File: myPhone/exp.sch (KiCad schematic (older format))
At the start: 19 parts, among them J301 iMX8

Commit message: upgrade to kicad 5; fixed footprints
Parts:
- C301, C302, C303, C304, C305, C306, C307, C308, C309, C310, C311, C312, C313, C314, C315, C316, C317, C318: footprint Capacitors_SMD:C_0603 -> Capacitor_SMD:C_0603_1608Metric; symbol C -> Device:C
- J301: symbol iMX8 -> SODIMM-204:iMX8

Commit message: REV1 board
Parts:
- added C319, C321, C325, C327, C337, C339: 1uF, Capacitor_SMD:C_0603_1608Metric, symbol Device:C_Small
- added C320, C322, C323, C326, C328, C329, C331, C333, C335, C338, C340: 0.1uF, Capacitor_SMD:C_0603_1608Metric, symbol Device:C_Small
- added C324, C330, C332, C334, C336: 0.01uF, Capacitor_SMD:C_0603_1608Metric, symbol Device:C_Small
- added C341, C342: 0.1uF, Capacitor_SMD:C_0603_1608Metric, symbol Device:C
- added J302: Touch, Connector_FFC-FPC:Hirose_FH12-6S-0.5SH_1x06-1MP_P0.50mm_Horizontal, symbol Connector_Generic:Conn_01x06
- added J303: Display, Connector_FFC-FPC:Hirose_FH12-40S-0.5SH_1x40-1MP_P0.50mm_Horizontal, symbol Connector_Generic:Conn_01x40
- added J304: Prog, Connector_FFC-FPC:Hirose_FH12-12S-0.5SH_1x12-1MP_P0.50mm_Horizontal, symbol Connector_Generic:Conn_01x12
- added R301: 4.7K, Resistor_SMD:R_0603_1608Metric, symbol Device:R
- added R302, R303: 1K, Resistor_SMD:R_0603_1608Metric, symbol Device:R
- added R304: 100K, Resistor_SMD:R_0603_1608Metric, symbol Device:R
- added U301: SN65LVDS822_SWAP, Package_DFN_QFN:QFN-48-1EP_7x7mm_P0.5mm_EP5.15x5.15mm_ThermalVias, symbol sn65:SN65LVDS822_SWAP
- added U302, U303, U304: TS3DDR3812, footprints:Texas_R-PWQFN-N42, symbol ts3ddr:TS3DDR3812
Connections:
- net GND: now also C319.2, C320.2, C321.2, C322.2, C323.2, C324.2, C325.2, C326.2, C327.2, C328.2, C329.2, C330.2, C331.2, C332.2, C333.2, C334.2, C335.2, C336.2, C337.2, C338.2, C339.2, C340.2, C341.2, C342.2, J302.6 (Pin_6), J303.29 (Pin_29), J303.3 (Pin_3), J303.36 (Pin_36), J304.3 (Pin_3), J304.9 (Pin_9), R304.2, U301.36 (MODE14), U301.49 (GND), U302.43 (GND), U303.43 (GND), U304.43 (GND)
- net iMX8_I2C1_SCL: now reaches J301.129 (PIN129)
- net iMX8_I2C1_SCL: now also U302.34 (B4)
- net iMX8_I2C1_SDA: now reaches J301.135 (PIN135)
- net iMX8_I2C1_SDA: now also U302.32 (B5)
- net iMX8_GPIO3_IO13: now reaches J301.149 (PIN149)
- net iMX8_GPIO3_IO13: now also U302.10 (SEL2), U302.9 (SEL1), U303.10 (SEL2), U303.9 (SEL1), U304.10 (SEL2), U304.9 (SEL1)
- net iMX8_GPIO3_IO12: now reaches J301.151 (PIN151)
- net iMX8_GPIO3_IO12: now also U302.38 (B2)
- net iMX8_GPIO3_IO11: now reaches J301.153 (PIN153)
- net iMX8_GPIO3_IO11: now also U302.36 (B3)
- net iMX8_USB1_D_P: now reaches J301.176 (PIN176)
- net iMX8_USB1_D_N: now reaches J301.178 (PIN178)
- net iMX8_LVDS0_CLK_P: now reaches J301.33 (PIN33)
- net iMX8_LVDS0_CLK_P: now also U301.32 (CLKP)
- net iMX8_LVDS0_CLK_N: now reaches J301.35 (PIN35)
- net iMX8_LVDS0_CLK_N: now also U301.31 (CLKN)
- net iMX8_LVDS0_A0_P: now reaches J301.39 (PIN39)
- net iMX8_LVDS0_A0_P: now also U301.26 (A0P)
- net iMX8_LVDS0_A0_N: now reaches J301.41 (PIN41)
- net iMX8_LVDS0_A0_N: now also U301.25 (A0N)
- net iMX8_LVDS0_A1_P: now reaches J301.45 (PIN45)
- net iMX8_LVDS0_A1_P: now also U301.28 (A1P)
- net iMX8_LVDS0_A1_N: now reaches J301.47 (PIN47)
- net iMX8_LVDS0_A1_N: now also U301.27 (A1N)
- net iMX8_GPIO5_IO28: now reaches J301.5 (PIN5)
- net iMX8_GPIO5_IO28: now also U304.25 (B8)
- net iMX8_LVDS0_A2_P: now reaches J301.51 (PIN51)
- net iMX8_LVDS0_A2_P: now also U301.30 (A2P)
- net iMX8_LVDS0_A2_N: now reaches J301.53 (PIN53)
- net iMX8_LVDS0_A2_N: now also U301.29 (A2N)
- net iMX8_LVDS0_A3_P: now reaches J301.57 (PIN57)
- net iMX8_LVDS0_A3_P: now also U301.34 (A3P)
- net iMX8_GPIO5_IO25: now reaches J301.58 (PIN58)
- net iMX8_GPIO5_IO25: now also U301.23 (CLKPOL)
- net iMX8_LVDS0_A3_N: now reaches J301.59 (PIN59)
- net iMX8_LVDS0_A3_N: now also U301.33 (A3N)
- net iMX8_PWM1: now reaches J301.75 (PIN75)
- net iMX8_PWM1: now also U302.29 (B6)
- net iMX8_GPIO2_IO17: now reaches J301.88 (PIN88)
- net iMX8_GPIO2_IO17: now also U301.35 (SLEW)
- net iMX8_GPIO2_IO18: now reaches J301.90 (PIN90)
- net iMX8_GPIO2_IO18: now also U301.37 (SHTDN#)
- new net +3V3: C319.1, C320.1, C321.1, C322.1, C323.1, C324.1, C325.1, C326.1, C327.1, C328.1, C329.1, C330.1, C331.1, C332.1, C333.1, C334.1, C335.1, C336.1, C337.1, C338.1, C339.1, C340.1, C341.1, C342.1, J302.3 (Pin_3), J303.4 (Pin_4), R301.1, R302.1, R303.1, U301.17 (VDDIO), U301.24 (VDD), U301.43 (VDDIO), U301.44 (VDD), U301.45 (SWAP), U301.6 (VDDIO), U302.1 (VCC), U302.17 (VCC), U302.30 (VCC), U302.8 (EN), U303.1 (VCC), U303.17 (VCC), U303.30 (VCC), U303.8 (EN), U304.1 (VCC), U304.17 (VCC), U304.30 (VCC), U304.8 (EN)
- new net BL_PWM: U302.11 (A6)
- new net CTP_INT: J302.5 (Pin_5), R301.2, U302.5 (A3)
- new net CTP_RST: J302.4 (Pin_4), R304.1, U302.4 (A2)
- new net CTP_SCL: J302.1 (Pin_1), R303.2, U302.6 (A4)
- new net CTP_SDA: J302.2 (Pin_2), R302.2, U302.7 (A5)
- new net DISP_B0: J303.21 (Pin_21), U303.16 (A11)
- new net DISP_B1: J303.22 (Pin_22), U304.2 (A0)
- new net DISP_B2: J303.23 (Pin_23), U304.3 (A1)
- new net DISP_B3: J303.24 (Pin_24), U304.4 (A2)
- new net DISP_B4: J303.25 (Pin_25), U304.5 (A3)
- new net DISP_B5: J303.26 (Pin_26), U304.6 (A4)
- new net DISP_B6: J303.27 (Pin_27), U304.7 (A5)
- new net DISP_B7: J303.28 (Pin_28), U304.11 (A6)
- new net DISP_DE: J303.34 (Pin_34), U304.16 (A11)
- new net DISP_EN: J303.31 (Pin_31), U304.13 (A8)
- new net DISP_G0: J303.13 (Pin_13), U303.5 (A3)
- new net DISP_G1: J303.14 (Pin_14), U303.6 (A4)
- new net DISP_G2: J303.15 (Pin_15), U303.7 (A5)
- new net DISP_G3: J303.16 (Pin_16), U303.11 (A6)
- new net DISP_G4: J303.17 (Pin_17), U303.12 (A7)
- new net DISP_G5: J303.18 (Pin_18), U303.13 (A8)
- new net DISP_G6: J303.19 (Pin_19), U303.14 (A9)
- new net DISP_G7: J303.20 (Pin_20), U303.15 (A10)
- new net DISP_HSYNC: J303.32 (Pin_32), U304.14 (A9)
- new net DISP_LED_A: J303.2 (Pin_2)
- new net DISP_LED_K: J303.1 (Pin_1)
- new net DISP_PCLK: J303.30 (Pin_30), U304.12 (A7)
- new net DISP_R0: J303.5 (Pin_5), U302.12 (A7)
- new net DISP_R1: J303.6 (Pin_6), U302.13 (A8)
- new net DISP_R2: J303.7 (Pin_7), U302.14 (A9)
- new net DISP_R3: J303.8 (Pin_8), U302.15 (A10)
- new net DISP_R4: J303.9 (Pin_9), U302.16 (A11)
- new net DISP_R5: J303.10 (Pin_10), U303.2 (A0)
- new net DISP_R6: J303.11 (Pin_11), U303.3 (A1)
- new net DISP_R7: J303.12 (Pin_12), U303.4 (A2)
- new net DISP_VSYNC: J303.33 (Pin_33), U304.15 (A10)
- new net ESP32.RXD0: J304.1 (Pin_1)
- new net ESP32.TXD0: J304.2 (Pin_2)
- new net FT813_B0: U303.18 (C11)
- new net FT813_B1: U304.42 (C0)
- new net FT813_B2: U304.40 (C1)
- new net FT813_B3: U304.37 (C2)
- new net FT813_B4: U304.35 (C3)
- new net FT813_B5: U304.33 (C4)
- new net FT813_B6: U304.31 (C5)
- new net FT813_B7: U304.28 (C6)
- new net FT813_BL_PWM: U302.28 (C6)
- new net FT813_CTP_INT: U302.35 (C3)
- new net FT813_CTP_RST: U302.37 (C2)
- new net FT813_CTP_SCL: U302.33 (C4)
- new net FT813_CTP_SDA: U302.31 (C5)
- new net FT813_DE: U304.18 (C11)
- new net FT813_DISP: U304.24 (C8)
- new net FT813_G0: U303.35 (C3)
- new net FT813_G1: U303.33 (C4)
- new net FT813_G2: U303.31 (C5)
- new net FT813_G3: U303.28 (C6)
- new net FT813_G4: U303.26 (C7)
- new net FT813_G5: U303.24 (C8)
- new net FT813_G6: U303.22 (C9)
- new net FT813_G7: U303.20 (C10)
- new net FT813_HSYNC: U304.22 (C9)
- new net FT813_PCLK: U304.26 (C7)
- new net FT813_R0: U302.26 (C7)
- new net FT813_R1: U302.24 (C8)
- new net FT813_R2: U302.22 (C9)
- new net FT813_R3: U302.20 (C10)
- new net FT813_R4: U302.18 (C11)
- new net FT813_R5: U303.42 (C0)
- new net FT813_R6: U303.40 (C1)
- new net FT813_R7: U303.37 (C2)
- new net FT813_VSYNC: U304.20 (C10)
- new net JTAG_TCK: J304.4 (Pin_4)
- new net JTAG_TDI: J304.7 (Pin_7)
- new net JTAG_TDO: J304.5 (Pin_5)
- new net JTAG_TMS: J304.6 (Pin_6)
- new net LVDS_B0: U301.11 (D12), U303.19 (B11)
- new net LVDS_B1: U301.12 (D13), U304.41 (B0)
- new net LVDS_B2: U301.13 (D14), U304.39 (B1)
- new net LVDS_B3: U301.14 (D15), U304.38 (B2)
- new net LVDS_B4: U301.15 (D16), U304.36 (B3)
- new net LVDS_B5: U301.16 (D17), U304.34 (B4)
- new net LVDS_B6: U301.18 (D25), U304.32 (B5)
- new net LVDS_B7: U301.19 (D26), U304.29 (B6)
- new net LVDS_CLKOUT: U301.41 (CLKOUT), U304.27 (B7)
- new net LVDS_DE: U301.22 (D20), U304.19 (B11)
- new net LVDS_G0: U301.2 (D6), U303.36 (B3)
- new net LVDS_G1: U301.3 (D7), U303.34 (B4)
- new net LVDS_G2: U301.4 (D8), U303.32 (B5)
- new net LVDS_G3: U301.5 (D9), U303.29 (B6)
- new net LVDS_G4: U301.7 (D10), U303.27 (B7)
- new net LVDS_G5: U301.8 (D11), U303.25 (B8)
- new net LVDS_G6: U301.9 (D23), U303.23 (B9)
- new net LVDS_G7: U301.10 (D24), U303.21 (B10)
- new net LVDS_HSYNC: U301.20 (D18), U304.23 (B9)
- new net LVDS_R0: U301.38 (D0), U302.27 (B7)
- new net LVDS_R1: U301.39 (D1), U302.25 (B8)
- new net LVDS_R2: U301.40 (D2), U302.23 (B9)
- new net LVDS_R3: U301.42 (D3), U302.21 (B10)
- new net LVDS_R4: U301.46 (D4), U302.19 (B11)
- new net LVDS_R5: U301.47 (D5), U303.41 (B0)
- new net LVDS_R6: U301.48 (D21), U303.39 (B1)
- new net LVDS_R7: U301.1 (D22), U303.38 (B2)
- new net LVDS_VSYNC: U301.21 (D19), U304.21 (B10)
- new net RESET: J304.8 (Pin_8)
- new net TPS.VOUT: J304.12 (Pin_12)
- new net UART0.RX: J304.11 (Pin_11)
- new net UART0.TX: J304.10 (Pin_10)
- no-connect marks 174 -> 164
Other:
- moved on the sheet: C302, C303, C304, C305, C306, C307, C308, C309, C310, C311, C312, C313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

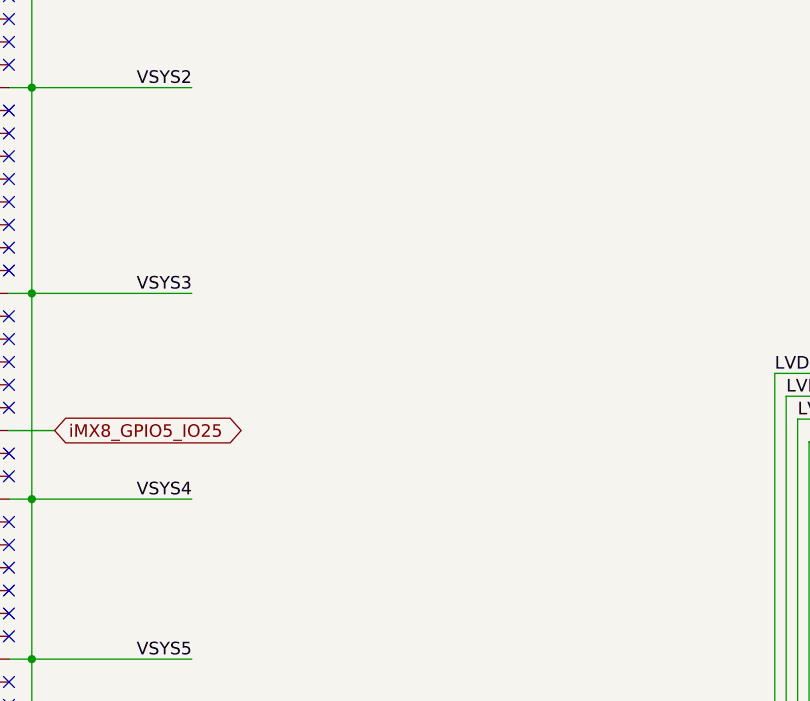
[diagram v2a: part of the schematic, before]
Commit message: display switch pull resistors added
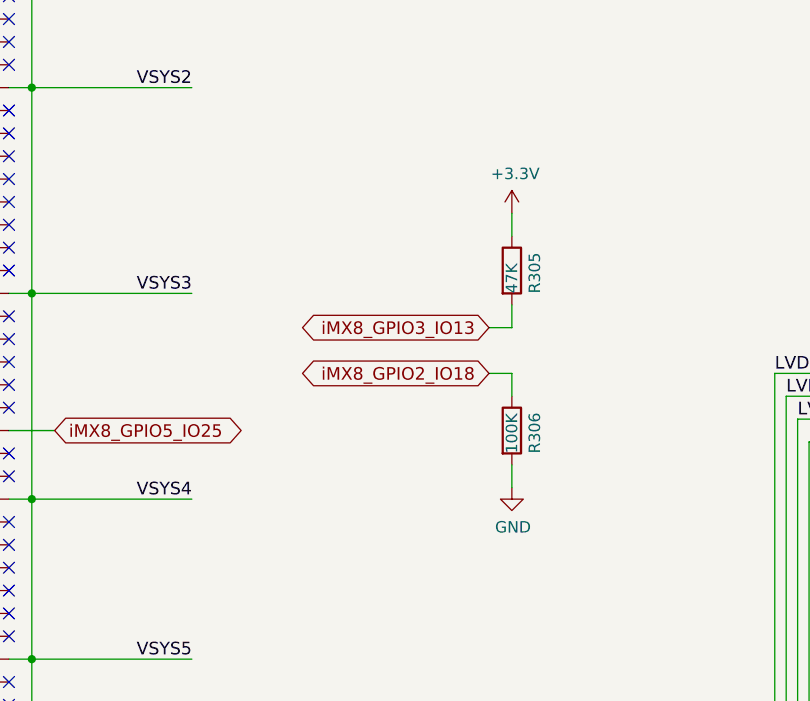
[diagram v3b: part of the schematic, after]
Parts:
- added R305: 47K, Resistor_SMD:R_0603_1608Metric, symbol Device:R
- added R306: 100K, Resistor_SMD:R_0603_1608Metric, symbol Device:R
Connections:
- net +3V3: now also R305.1
- net GND: now also R306.2
- net iMX8_GPIO2_IO18: now also R306.1
- net iMX8_GPIO3_IO13: now also R305.2
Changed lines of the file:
@@
 Wire Wire Line
 	10950 3950 11300 3950
+Text GLabel 5100 3350 0    55   BiDi ~ 0
+iMX8_GPIO2_IO18
+Text GLabel 5100 3150 0    55   BiDi ~ 0
+iMX8_GPIO3_IO13
+$Comp
+L Device:R R305
+U 1 1 5DB02E01
+P 5200 2900
+F 0 "R305" V 5300 2800 50  0000 L CNN
+F 1 "47K" V 5200 2800 50  0000 L CNN
+F 2 "Resistor_SMD:R_0603_1608Metric" V 5130 2900 50  0001 C CNN
+F 3 "~" H 5200 2900 50  0001 C CNN
+	1    5200 2900
+	1    0    0    -1
+$EndComp
+$Comp
+L Device:R R306
+U 1 1 5DB0397A
+P 5200 3600
+F 0 "R306" V 5300 3500 50  0000 L CNN
+F 1 "100K" V 5200 3500 50  0000 L CNN
+F 2 "Resistor_SMD:R_0603_1608Metric" V 5130 3600 50  0001 C CNN
+F 3 "~" H 5200 3600 50  0001 C CNN
+	1    5200 3600
+	1    0    0    -1
+$EndComp
+$Comp
+L power:+3.3V #PWR0313
+U 1 1 5DB043CD
+P 5200 2650
+F 0 "#PWR0313" H 5200 2500 50  0001 C CNN
+F 1 "+3.3V" H 5215 2823 50  0000 C CNN
+F 2 "" H 5200 2650 50  0001 C CNN
+F 3 "" H 5200 2650 50  0001 C CNN
+	1    5200 2650
+	1    0    0    -1
+$EndComp
+$Comp
+L power:GND #PWR0314
+U 1 1 5DB04E76
+P 5200 3850
+F 0 "#PWR0314" H 5200 3600 50  0001 C CNN
+F 1 "GND" H 5205 3677 50  0000 C CNN
+F 2 "" H 5200 3850 50  0001 C CNN
+F 3 "" H 5200 3850 50  0001 C CNN
+	1    5200 3850
+	1    0    0    -1
+$EndComp
+Wire Wire Line
+	5100 3350 5200 3350
+Wire Wire Line
+	5200 3350 5200 3450
+Wire Wire Line
+	5100 3150 5200 3150
+Wire Wire Line
+	5200 3150 5200 3050
+Wire Wire Line
+	5200 3750 5200 3850
+Wire Wire Line
+	5200 2750 5200 2650
 $EndSCHEMATC

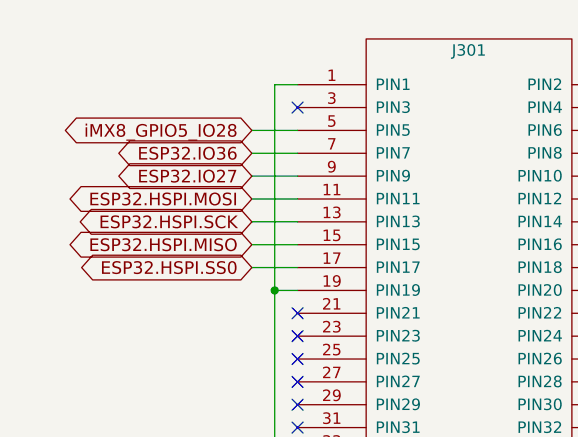
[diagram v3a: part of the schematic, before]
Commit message: fixed battery charger; added i2c switch for fe310; swapped pwm1/pwm2 for mic/spk
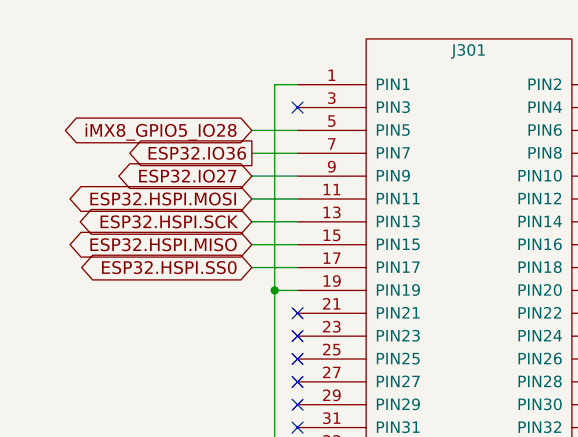
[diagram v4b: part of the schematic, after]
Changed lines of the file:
@@
 Wire Wire Line
 	12600 850  12300 850
-Text GLabel 1300 1100 0    55   BiDi ~ 0
+Text GLabel 1300 1100 0    55   Output ~ 0
 ESP32.IO36
 Text GLabel 1300 1200 0    55   BiDi ~ 0
